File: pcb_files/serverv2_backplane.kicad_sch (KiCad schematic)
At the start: 0 parts

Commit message: Changed TPS55288 to internal droop compensation and added current monitoring for TPS55288 to ADC pin of LicheeRV Nano
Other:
- sheet PAC1954_PSU_PD ports: added none; removed VBUS, VBUS_SENSE
- sheet SG2002_HEADER ports: added ADC; removed none
- sheet TPS55288 ports: added I_MONITOR; removed none
- sheet Upstream_USB-C ports: added VBUS; removed VBUS_SENSE
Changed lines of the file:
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@@
 	(wire
 		(pts
+			(xy 116.84 77.47) (xy 116.84 72.39)
+		)
+		(stroke
+			(width 0)
+			(type default)
+		)
+	)
+	(wire
+		(pts
 			(xy 182.88 252.73) (xy 199.39 252.73)
 		)
@@
 	(wire
 		(pts
+			(xy 163.83 138.43) (xy 163.83 179.07)
+		)
+		(stroke
+			(width 0)
+			(type default)
+		)
+	)
+	(wire
+		(pts
 			(xy 182.88 364.49) (xy 199.39 364.49)
 		)
@@
 	(wire
 		(pts
-			(xy 139.7 58.42) (xy 138.43 58.42)
+			(xy 139.7 55.88) (xy 138.43 55.88)
 		)
 		(stroke
@@
 	(wire
 		(pts
-			(xy 116.84 69.85) (xy 116.84 77.47)
-		)
-		(stroke
-			(width 0)
-			(type default)
-			(color 193 0 0 1)
-		)
-	)
-	(wire
-		(pts
 			(xy 316.23 412.75) (xy 356.87 412.75)
 		)
@@
 	(wire
 		(pts
-			(xy 44.45 66.04) (xy 90.17 66.04)
-		)
-		(stroke
-			(width 0)
-			(type default)
-			(color 193 0 0 1)
-		)
-	)
-	(wire
-		(pts
 			(xy 242.57 153.67) (xy 233.68 153.67)
 		)
@@
 	(wire
 		(pts
-			(xy 139.7 60.96) (xy 138.43 60.96)
+			(xy 139.7 58.42) (xy 138.43 58.42)
 		)
 		(stroke
@@
 	(wire
 		(pts
+			(xy 163.83 179.07) (xy 261.62 179.07)
+		)
+		(stroke
+			(width 0)
+			(type default)
+		)
+	)
+	(wire
+		(pts
 			(xy 151.13 496.57) (xy 152.4 496.57)
 		)
@@
 	(wire
 		(pts
+			(xy 261.62 179.07) (xy 261.62 186.69)
+		)
+		(stroke
+			(width 0)
+			(type default)
+		)
+	)
+	(wire
+		(pts
 			(xy 119.38 255.27) (xy 152.4 255.27)
 		)
@@
 	(wire
 		(pts
+			(xy 261.62 186.69) (xy 257.81 186.69)
+		)
+		(stroke
+			(width 0)
+			(type default)
+		)
+	)
+	(wire
+		(pts
 			(xy 389.255 78.74) (xy 398.78 78.74)
 		)
@@
 	(wire
 		(pts
+			(xy 116.84 72.39) (xy 44.45 72.39)
+		)
+		(stroke
+			(width 0)
+			(type default)
+		)
+	)
+	(wire
+		(pts
 			(xy 237.49 240.03) (xy 240.03 240.03)
 		)
@@
 	(wire
 		(pts
-			(xy 139.7 138.43) (xy 138.43 138.43)
+			(xy 139.7 134.62) (xy 138.43 134.62)
 		)
 		(stroke
@@
 	(wire
 		(pts
-			(xy 138.43 66.04) (xy 142.24 66.04)
+			(xy 138.43 62.23) (xy 142.24 62.23)
 		)
 		(stroke
@@
 	(wire
 		(pts
+			(xy 138.43 138.43) (xy 163.83 138.43)
+		)
+		(stroke
+			(width 0)
+			(type default)
+		)
+	)
+	(wire
+		(pts
 			(xy 148.59 382.27) (xy 152.4 382.27)
 		)
@@
 	(global_label "PWR_BTN"
 		(shape output)
-		(at 139.7 138.43 0)
+		(at 139.7 134.62 0)
 		(fields_autoplaced yes)
 		(effects
@@
 		)
 		(property "Intersheetrefs" "${INTERSHEET_REFS}"
-			(at 151.2123 138.43 0)
+			(at 151.2123 134.62 0)
 			(hide yes)
 			(show_name no)
@@
 	(global_label "SDA3"
 		(shape bidirectional)
-		(at 139.7 60.96 0)
+		(at 139.7 58.42 0)
 		(fields_autoplaced yes)
 		(effects
@@
 		)
 		(property "Intersheetrefs" "${INTERSHEET_REFS}"
-			(at 148.5741 60.96 0)
+			(at 148.5741 58.42 0)
 			(hide yes)
 			(show_name no)
@@
 	(global_label "SCL3"
 		(shape input)
-		(at 139.7 58.42 0)
+		(at 139.7 55.88 0)
 		(fields_autoplaced yes)
 		(effects
@@
 		)
 		(property "Intersheetrefs" "${INTERSHEET_REFS}"
-			(at 147.4023 58.42 0)
+			(at 147.4023 55.88 0)
 			(hide yes)
 			(show_name no)
@@
 	(symbol
 		(lib_id "power:GND")
-		(at 142.24 66.04 0)
+		(at 142.24 62.23 0)
 		(unit 1)
 		(body_style 1)
@@
 		(fields_autoplaced yes)
 		(property "Reference" "#PWR022"
-			(at 142.24 72.39 0)
+			(at 142.24 68.58 0)
 			(hide yes)
 			(show_name no)
@@
 		)
 		(property "Value" "GND"
-			(at 142.24 71.12 0)
+			(at 142.24 67.31 0)
 			(show_name no)
 			(do_not_autoplace no)
@@
 		)
 		(property "Footprint" ""
-			(at 142.24 66.04 0)
+			(at 142.24 62.23 0)
 			(hide yes)
 			(show_name no)
@@
 		)
 		(property "Datasheet" ""
-			(at 142.24 66.04 0)
+			(at 142.24 62.23 0)
 			(hide yes)
 			(show_name no)
@@
 		)
 		(property "Description" "Power symbol creates a global label with name \"GND\" , ground"
-			(at 142.24 66.04 0)
+			(at 142.24 62.23 0)
 			(hide yes)
 			(show_name no)
@@
 			)
 		)
-		(pin "VBUS_SENSE" input
-			(at 44.45 66.04 0)
+		(pin "VBUS" input
+			(at 44.45 72.39 0)
 			(effects
 				(font
@@
 		)
 		(pin "PWR_FAULT" output
-			(at 138.43 138.43 0)
+			(at 138.43 134.62 0)
 			(effects
 				(font
@@
 			)
 		)
+		(pin "I_MONITOR" output
+			(at 138.43 138.43 0)
+			(effects
+				(font
+					(size 1.27 1.27)
+				)
+				(justify right)
+			)
+		)
 		(instances
 			(project "serverv2_backplane"
@@
 	(sheet
 		(at 90.17 43.18)
-		(size 48.26 26.67)
+		(size 48.26 23.622)
 		(exclude_from_sim no)
 		(in_bom yes)
@@
 		)
 		(property "Sheetfile" "PAC1954_PSU_PD.kicad_sch"
-			(at 90.17 70.4346 0)
+			(at 90.17 67.3866 0)
 			(hide yes)
 			(show_name no)
@@
 			)
 		)
-		(pin "VBUS_SENSE" output
-			(at 90.17 66.04 180)
-			(effects
-				(font
-					(size 1.27 1.27)
-				)
-				(justify left)
-			)
-		)
 		(pin "+5V" output
 			(at 138.43 49.53 0)
@@
 			)
 		)
-		(pin "VBUS" input
-			(at 116.84 69.85 270)
-			(effects
-				(font
-					(size 1.27 1.27)
-				)
-				(justify left)
-			)
-		)
 		(pin "+3V3" output
 			(at 138.43 46.99 0)
@@
 		)
 		(pin "SCL" input
-			(at 138.43 58.42 0)
+			(at 138.43 55.88 0)
 			(effects
 				(font
@@
 		)
 		(pin "SDA" bidirectional
-			(at 138.43 60.96 0)
+			(at 138.43 58.42 0)
 			(effects
 				(font
@@
 		)
 		(pin "GND" input
-			(at 138.43 66.04 0)
+			(at 138.43 62.23 0)
 			(effects
 				(font
@@
 			)
 		)
+		(pin "ADC" input
+			(at 257.81 186.69 0)
+			(effects
+				(font
+					(size 1.27 1.27)
+				)
+				(justify right)
+			)
+		)

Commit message: Switched PAC1954 to SLOW mode to save power
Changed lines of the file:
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@@
 			)
 		)
-		(pin "+3V3" output
+		(pin "+3V3" input
 			(at 138.43 46.99 0)
 			(effects

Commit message: Added FAN4 and updated RP2354/PAC1954 to match
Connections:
- no-connect marks 13 -> 17
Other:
- added sheet FAN_HEADER_4 (FAN_HEADER.kicad_sch)
- sheet PAC1954_FANS ports: added GND; removed none
- sheet PAC1954_HUB ports: added VDD; removed +3V3
- sheet PAC1954_PSU_PD ports: added +12V_FAN4, VDD; removed +3V3
- sheet RP2354B_0 ports: added GPIO10_PWM5A, GPIO11; removed none
- sheet RP2354B_1 ports: added GPIO10_PWM5A, GPIO11; removed none
- sheet RP2354B_2 ports: added GPIO10_PWM5A, GPIO11; removed none
- note added: "FAN_PWM_4"
- note added: "FAN_TACH_4"

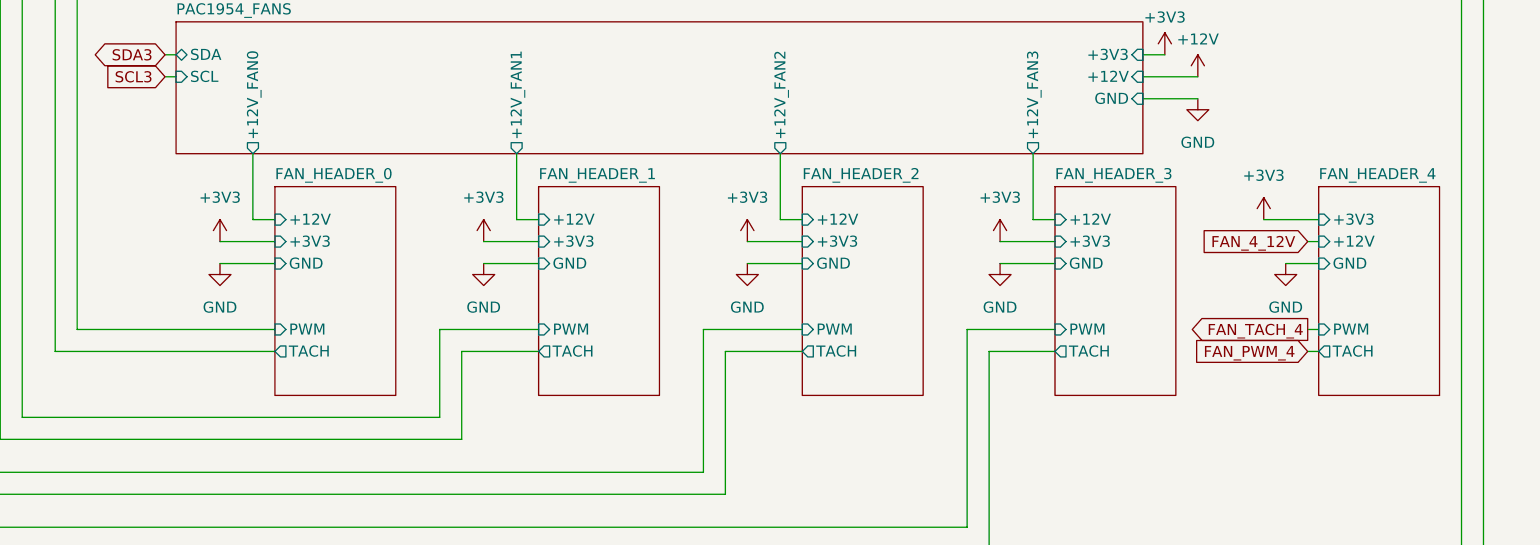
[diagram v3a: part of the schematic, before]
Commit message: Added ESD protection to fans
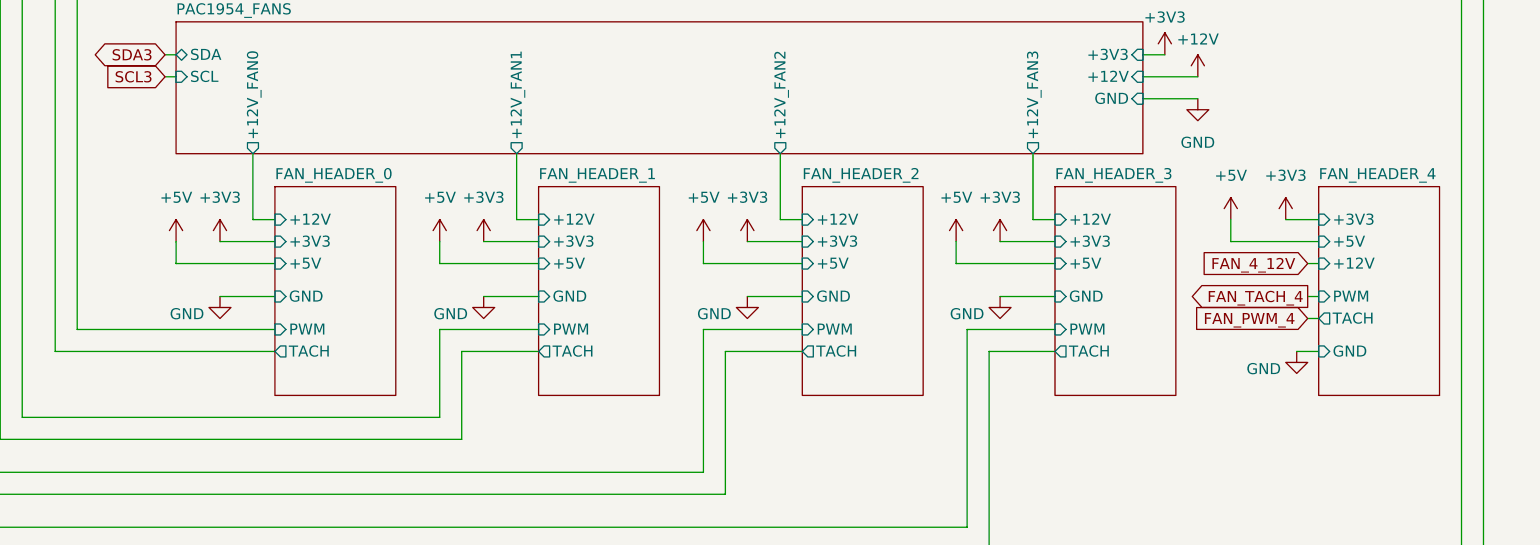
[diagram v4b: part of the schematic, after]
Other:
- sheet FAN_HEADER_0 ports: added +5V; removed none
- sheet FAN_HEADER_1 ports: added +5V; removed none
- sheet FAN_HEADER_2 ports: added +5V; removed none
- sheet FAN_HEADER_3 ports: added +5V; removed none
- sheet FAN_HEADER_4 ports: added +5V; removed none

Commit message: Basic Function Review/Documentation for PSU PAC1954
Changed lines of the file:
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@@
 	(wire
 		(pts
-			(xy 116.84 77.47) (xy 116.84 72.39)
-		)
-		(stroke
-			(width 0)
-			(type default)
-		)
-	)
-	(wire
-		(pts
 			(xy 182.88 252.73) (xy 199.39 252.73)
 		)
@@
 	(wire
 		(pts
-			(xy 116.84 72.39) (xy 44.45 72.39)
+			(xy 90.17 87.63) (xy 44.45 87.63)
 		)
 		(stroke
@@
 		)
 		(pin "VBUS" input
-			(at 44.45 72.39 0)
+			(at 44.45 87.63 0)
 			(effects
 				(font
@@
 		)
 		(pin "VBUS" output
-			(at 116.84 77.47 90)
+			(at 90.17 87.63 180)
 			(effects
 				(font
 					(size 1.27 1.27)
 				)
-				(justify right)
+				(justify left)
 			)
 		)
